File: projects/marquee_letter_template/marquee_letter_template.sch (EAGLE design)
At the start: 54 parts, among them Q1 BSH103

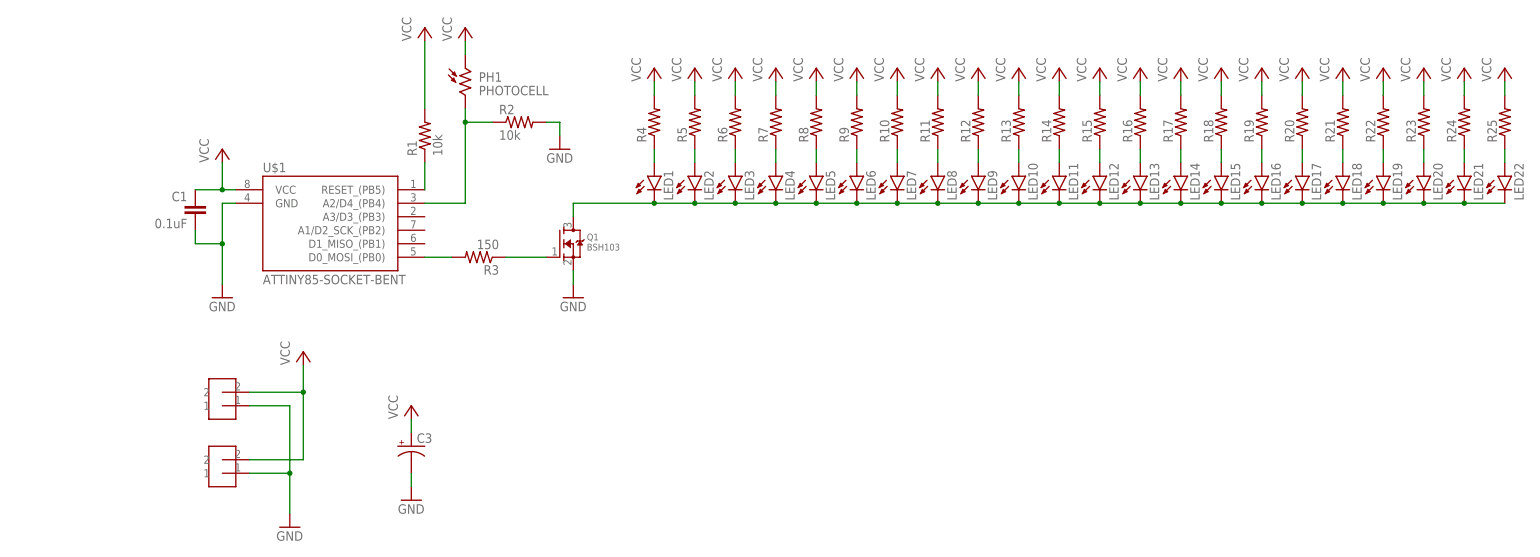
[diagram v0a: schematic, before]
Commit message: create marquee letter template; adds image and gif of example board
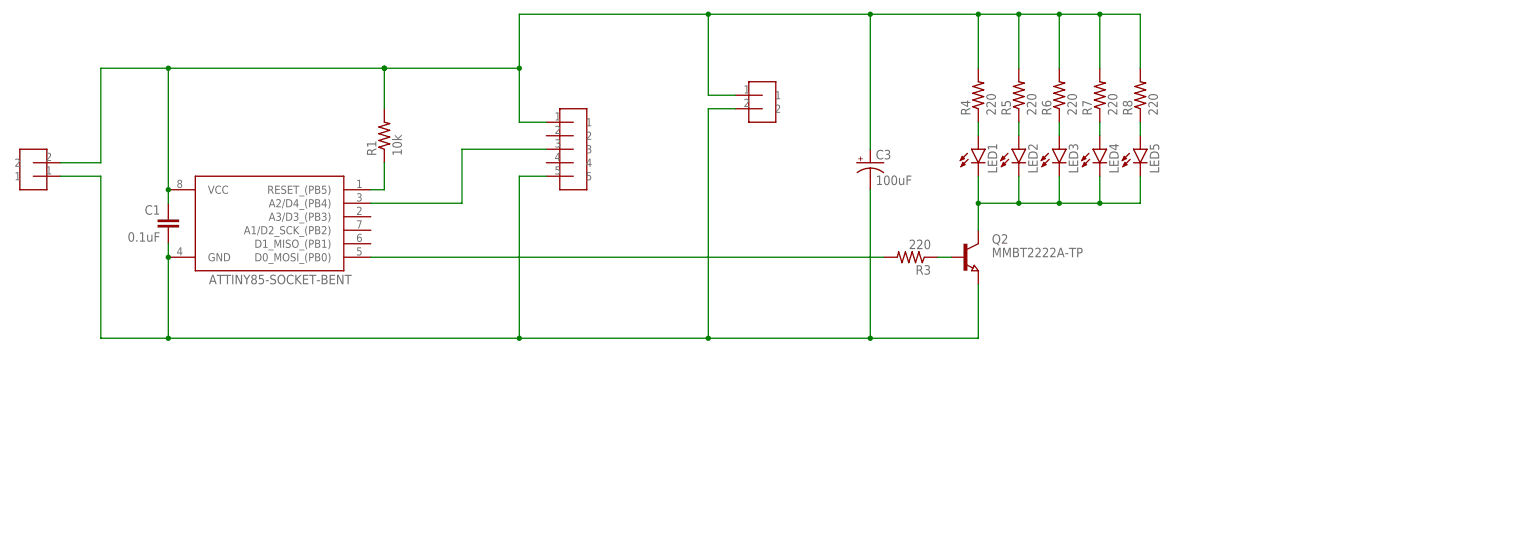
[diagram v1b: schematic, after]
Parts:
- removed LED10, LED11, LED12, LED13, LED14, LED15, LED16, LED17, LED18, LED19, LED20, LED21, LED22, LED6, LED7, LED8, LED9: (no value), homemade-hardware:LED0603
- removed PH1: PHOTOCELL, homemade-hardware:PHOTOCELL
- removed Q1: BSH103, adafruit:MOSFET-NREFLOW
- removed R10, R11, R12, R13, R14, R15, R16, R17, R18, R19, R20, R21, R22, R23, R24, R25, R9: (no value), homemade-hardware:RESISTOR0603
- removed R2: 10k, homemade-hardware:RESISTOR-0805
- added POTENTIOMETER: HEADER-5, homemade-hardware:HEADER-5
- added Q2: MMBT2222A-TP, homemade-hardware:TRANSISTOR-NPN-SOT23
- C3: value (none) -> 100uF
- R3: value 150 -> 220
- R4, R5, R6, R7, R8: value (none) -> 220
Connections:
- net RESET renamed N$12
- removed net GND_LED: LED1.C, LED10.C, LED11.C, LED12.C, LED13.C, LED14.C, LED15.C, LED16.C, LED17.C, LED18.C, LED19.C, LED2.C, LED20.C, LED21.C, LED22.C, LED3.C, LED4.C, LED5.C, LED6.C, LED7.C, LED8.C, LED9.C, Q1.D
- removed net N$11: LED6.A, R9.1
- removed net N$12 (its old number): LED7.A, R10.1
- removed net N$13: LED8.A, R11.1
- removed net N$14: LED9.A, R12.1
- removed net N$15: LED10.A, R13.1
- removed net N$16: LED11.A, R14.1
- removed net N$17: LED12.A, R15.1
- removed net N$18: LED13.A, R16.1
- removed net N$19: LED14.A, R17.1
- removed net N$20: LED15.A, R18.1
- removed net N$21: LED16.A, R19.1
- removed net N$22: LED17.A, R20.1
- removed net N$23: LED18.A, R21.1
- removed net N$24: LED19.A, R22.1
- removed net N$25: LED20.A, R23.1
- removed net N$26: LED21.A, R24.1
- removed net N$27: LED22.A, R25.1
- removed net VCC: C1.1, C3.+, PH1.1, R1.2, R10.2, R11.2, R12.2, R13.2, R14.2, R15.2, R16.2, R17.2, R18.2, R19.2, R20.2, R21.2, R22.2, R23.2, R24.2, R25.2, R4.2, R5.2, R6.2, R7.2, R8.2, R9.2, U$1.VCC, U$2.2, U$3.2
- new net 5V: C1.1, C3.+, POTENTIOMETER.1, R1.2, R4.2, R5.2, R6.2, R7.2, R8.2, U$1.VCC, U$2.2, U$3.1
- new net N$4: LED1.C, LED2.C, LED3.C, LED4.C, LED5.C, Q2.C
- net GND: now also POTENTIOMETER.5, Q2.E, U$3.2; no longer Q1.S, R2.2, U$3.1
- net N$5: now also Q2.B; no longer Q1.G
- net SENSOR: now also POTENTIOMETER.3; no longer PH1.2, R2.1
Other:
- note added: "5V"
- note added: "Copy/Paste to add more LEDs --->>"
- note added: "FYI: Not Connected (because no dot)"
- note added: "GND"
- note added: "Large Capacitor (for LED power surges)"
- note added: "NPN Transistor"
- note added: "Potentiometer (change header for different sensors)"
- note added: "Power In"
- note added: "Power Out (to next letter)"
- moved on the sheet: C1, C3, LED1, LED2, LED3, LED4, LED5, R1, R3, R4, R5, R6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
